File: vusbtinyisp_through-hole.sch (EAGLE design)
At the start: 9 parts, among them U1 Tiny85-20-SMT

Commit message: complete, untested dip version
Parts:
- removed U$1: SMT_ISP, elliot:SMT_ISP
- added J1: AVR_SPI_PRG_6NS, SparkFun-Connectors:AVR_SPI_PRG_6NS
- C1: device SparkFun-Passives:CAP1206 -> SparkFun-Passives:CAPPTH
- D1, D2: device diode:ZENER-DIODESOT23 -> diode:ZENER-DIODEDO35Z10
- R1, R2: device resistor:R-EU_R0805 -> resistor:R-EU_0207/10
- R3: device resistor:R-EU_R1206 -> resistor:R-EU_0207/10
- U1: value Tiny85-20-SMT -> TINY45-20-DIP; device SparkFun-DigitalIC:ATTINY45TINY85-20-SMT -> SparkFun-DigitalIC:ATTINY45TINY45-20-DIP
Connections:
- net GND: now also J1.6; no longer U$1.GND
- net MISO: now also J1.1; no longer U$1.MISO
- net MOSI: now also J1.4; no longer U$1.MOSI
- net RESET: now also J1.5; no longer U$1.RESET
- net SCK: now also J1.3; no longer U$1.SCK
- net VCC: now also J1.2; no longer U$1.VCC

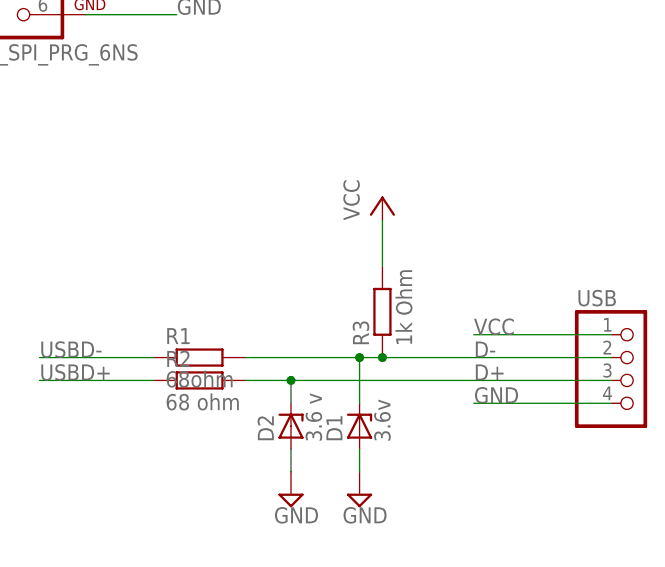
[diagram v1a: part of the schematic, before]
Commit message: changing 1k to 1.5k resistors in 5V designs
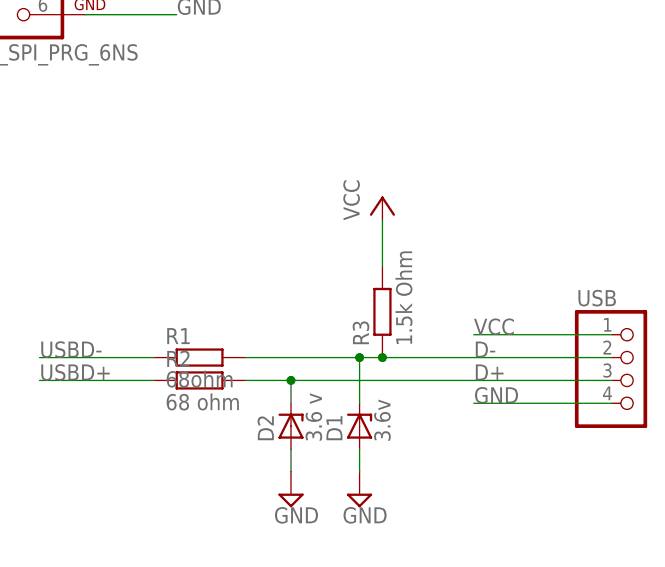
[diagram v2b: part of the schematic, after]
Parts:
- R3: value 1k Ohm -> 1.5k Ohm
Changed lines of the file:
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@@
 <grid distance="0.1" unitdist="inch" unit="inch" style="lines" multiple="1" display="no" altdistance="0.01" altunitdist="inch" altunit="inch"/>
 <layers>
-<layer number="1" name="Top" color="4" fill="1" visible="yes" active="no"/>
-<layer number="16" name="Bottom" color="1" fill="1" visible="yes" active="no"/>
-<layer number="17" name="Pads" color="2" fill="1" visible="yes" active="no"/>
-<layer number="18" name="Vias" color="2" fill="1" visible="yes" active="no"/>
-<layer number="19" name="Unrouted" color="6" fill="1" visible="yes" active="no"/>
-<layer number="20" name="Dimension" color="15" fill="1" visible="yes" active="no"/>
-<layer number="21" name="tPlace" color="7" fill="1" visible="yes" active="no"/>
-<layer number="22" name="bPlace" color="7" fill="1" visible="yes" active="no"/>
-<layer number="23" name="tOrigins" color="15" fill="1" visible="yes" active="no"/>
-<layer number="24" name="bOrigins" color="15" fill="1" visible="yes" active="no"/>
-<layer number="25" name="tNames" color="7" fill="1" visible="yes" active="no"/>
-<layer number="26" name="bNames" color="7" fill="1" visible="yes" active="no"/>
-<layer number="27" name="tValues" color="7" fill="1" visible="yes" active="no"/>
-<layer number="28" name="bValues" color="7" fill="1" visible="yes" active="no"/>
+<layer number="1" name="Top" color="4" fill="1" visible="no" active="no"/>
+<layer number="16" name="Bottom" color="1" fill="1" visible="no" active="no"/>
+<layer number="17" name="Pads" color="2" fill="1" visible="no" active="no"/>
+<layer number="18" name="Vias" color="2" fill="1" visible="no" active="no"/>
+<layer number="19" name="Unrouted" color="6" fill="1" visible="no" active="no"/>
+<layer number="20" name="Dimension" color="15" fill="1" visible="no" active="no"/>
+<layer number="21" name="tPlace" color="7" fill="1" visible="no" active="no"/>
+<layer number="22" name="bPlace" color="7" fill="1" visible="no" active="no"/>
+<layer number="23" name="tOrigins" color="15" fill="1" visible="no" active="no"/>
+<layer number="24" name="bOrigins" color="15" fill="1" visible="no" active="no"/>
+<layer number="25" name="tNames" color="7" fill="1" visible="no" active="no"/>
+<layer number="26" name="bNames" color="7" fill="1" visible="no" active="no"/>
+<layer number="27" name="tValues" color="7" fill="1" visible="no" active="no"/>
+<layer number="28" name="bValues" color="7" fill="1" visible="no" active="no"/>
 <layer number="29" name="tStop" color="7" fill="3" visible="no" active="no"/>
 <layer number="30" name="bStop" color="7" fill="6" visible="no" active="no"/>
@@
 <layer number="35" name="tGlue" color="7" fill="4" visible="no" active="no"/>
 <layer number="36" name="bGlue" color="7" fill="5" visible="no" active="no"/>
-<layer number="37" name="tTest" color="7" fill="1" visible="yes" active="no"/>
-<layer number="38" name="bTest" color="7" fill="1" visible="yes" active="no"/>
+<layer number="37" name="tTest" color="7" fill="1" visible="no" active="no"/>
+<layer number="38" name="bTest" color="7" fill="1" visible="no" active="no"/>
 <layer number="39" name="tKeepout" color="4" fill="11" visible="no" active="no"/>
 <layer number="40" name="bKeepout" color="1" fill="11" visible="no" active="no"/>
@@
 <layer number="44" name="Drills" color="7" fill="1" visible="no" active="no"/>
 <layer number="45" name="Holes" color="7" fill="1" visible="no" active="no"/>
-<layer number="46" name="Milling" color="3" fill="1" visible="yes" active="no"/>
-<layer number="47" name="Measures" color="7" fill="1" visible="yes" active="no"/>
-<layer number="48" name="Document" color="7" fill="1" visible="yes" active="no"/>
-<layer number="49" name="Reference" color="7" fill="1" visible="yes" active="no"/>
-<layer number="50" name="dxf" color="7" fill="1" visible="yes" active="no"/>
-<layer number="51" name="tDocu" color="7" fill="1" visible="yes" active="no"/>
-<layer number="52" name="bDocu" color="7" fill="1" visible="yes" active="no"/>
-<layer number="53" name="tGND_GNDA" color="7" fill="9" visible="yes" active="no"/>
-<layer number="54" name="bGND_GNDA" color="1" fill="9" visible="yes" active="no"/>
-<layer number="56" name="wert" color="7" fill="1" visible="yes" active="no"/>
+<layer number="46" name="Milling" color="3" fill="1" visible="no" active="no"/>
+<layer number="47" name="Measures" color="7" fill="1" visible="no" active="no"/>
+<layer number="48" name="Document" color="7" fill="1" visible="no" active="no"/>
+<layer number="49" name="Reference" color="7" fill="1" visible="no" active="no"/>
+<layer number="50" name="dxf" color="7" fill="1" visible="no" active="no"/>
+<layer number="51" name="tDocu" color="7" fill="1" visible="no" active="no"/>
+<layer number="52" name="bDocu" color="7" fill="1" visible="no" active="no"/>
+<layer number="53" name="tGND_GNDA" color="7" fill="9" visible="no" active="no"/>
+<layer number="54" name="bGND_GNDA" color="1" fill="9" visible="no" active="no"/>
+<layer number="56" name="wert" color="7" fill="1" visible="no" active="no"/>
 <layer number="91" name="Nets" color="2" fill="1" visible="yes" active="yes"/>
 <layer number="92" name="Busses" color="1" fill="1" visible="yes" active="yes"/>
@@
 <part name="SUPPLY3" library="supply2" deviceset="GND" device=""/>
 <part name="P+2" library="supply1" deviceset="VCC" device=""/>
-<part name="R3" library="resistor" deviceset="R-EU_" device="0207/10" value="1k Ohm"/>
+<part name="R3" library="resistor" deviceset="R-EU_" device="0207/10" value="1.5k Ohm"/>
 <part name="J1" library="SparkFun-Connectors" deviceset="AVR_SPI_PRG_6" device="NS"/>
 </parts>
